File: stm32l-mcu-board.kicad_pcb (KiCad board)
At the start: 4 copper layers, 28 x 45 mm, 59 parts, among them J1 CON_USB_GCT_USB4105_REVA, J2 PROG, J3 PORT, J4 PORT, Q1 MIC94052YC6-TR, SW1 SW_Push, SW2 SW_Push, U1 IC-SENSOR-TEMP-HUM-SHT4X, U2 W25Q16JVSNIQ, U3 STM32L151CCTx, U4 ADXL343, U5 MCP9701T-E/TT, U6 CH340C, U7 TC1264-3.3VDBTR, Y1 16MHz

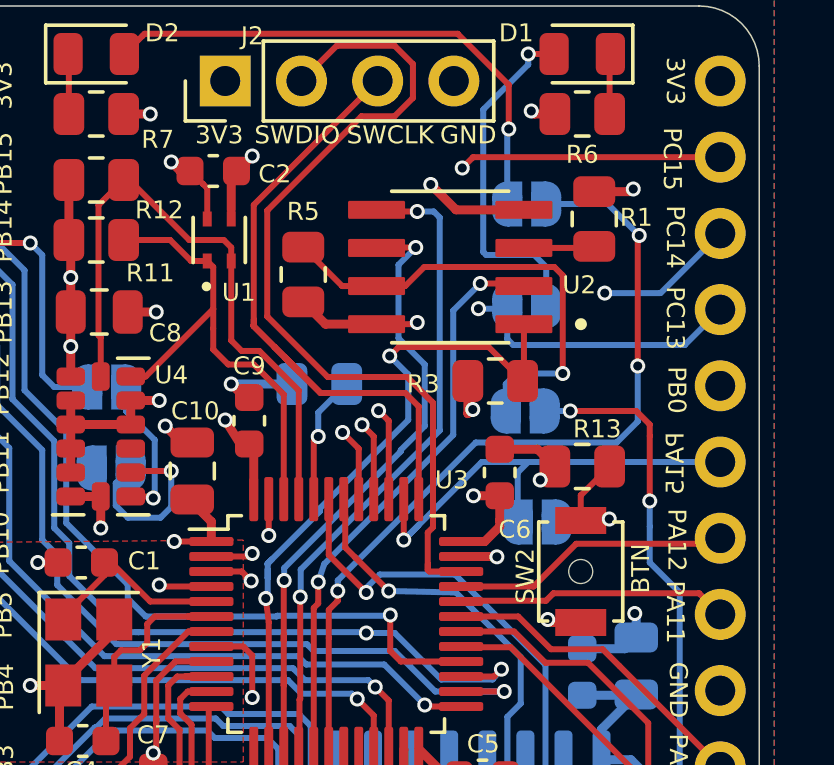
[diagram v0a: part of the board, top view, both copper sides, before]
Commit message: Update the Flash memory circuit
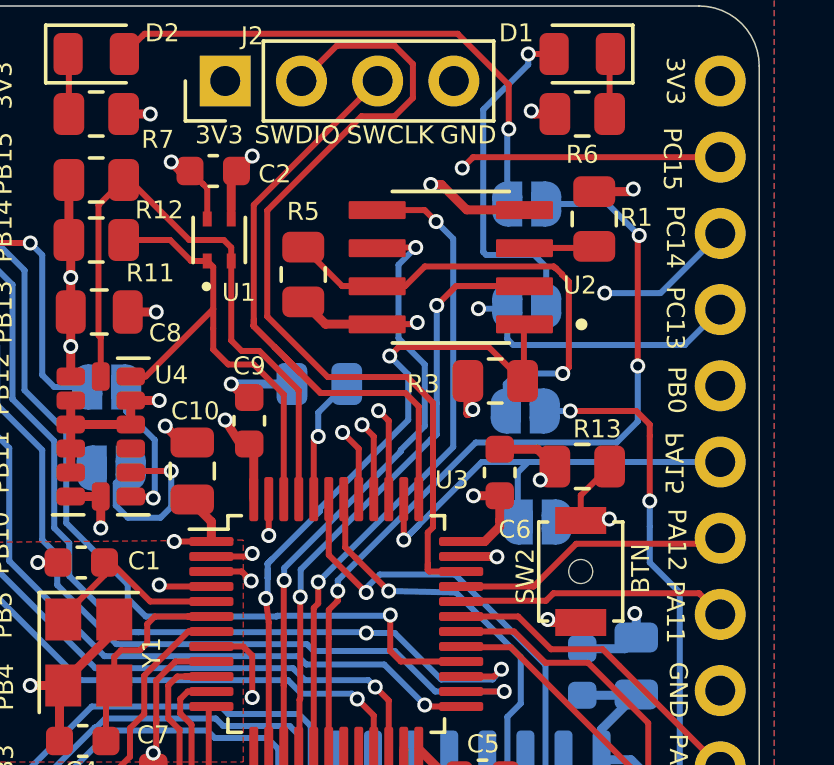
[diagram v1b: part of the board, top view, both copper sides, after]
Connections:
- U3 pad 16: DI -> DO
- U3 pad 17: DO -> DI
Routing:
- net DO: track 19.3 -> 20.0 mm
